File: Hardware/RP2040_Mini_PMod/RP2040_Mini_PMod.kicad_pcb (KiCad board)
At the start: 4 copper layers, 50 x 20 mm, 39 parts, among them J3 Conn_02x06_Odd_Even, J4 USB_C_Receptacle_USB2.0, J5 Conn_01x04, SW1 SW_Push, SW2 SW_Push, U1 RP2040, U2 W25Q128JVS, U3 NCP1117-3.3_SOT223, Y1 12MHz

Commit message: continue with mini project
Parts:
- added J1: Micro_SD_Card, jjh:105162-0001, B.Cu at (149.5, 104.2)
- SW1, SW2: footprint Button_Switch_THT:SW_PUSH_6mm_H4.3mm -> jjh:PTS815SJK250SMTRLFS
- moved SW2 54.8 mm to (166.9, 111.7)
- moved SW1 31.1 mm to (166.9, 96.4)
- moved R2 27.3 mm to (162.9, 96.6), turned to 90 degrees
- moved J3 9.30 mm to (172.3, 97.3)
- moved C2 5.61 mm to (168.5, 107.9), turned to 180 degrees
- moved R1 4.95 mm to (168.5, 100.3), turned to 180 degrees
- moved C4 4.95 mm to (168.5, 101.9)
- moved Y1 1.36 mm to (168.5, 104.9), turned to 90 degrees
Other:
- board size 50 x 20 mm -> 40 x 20 mm

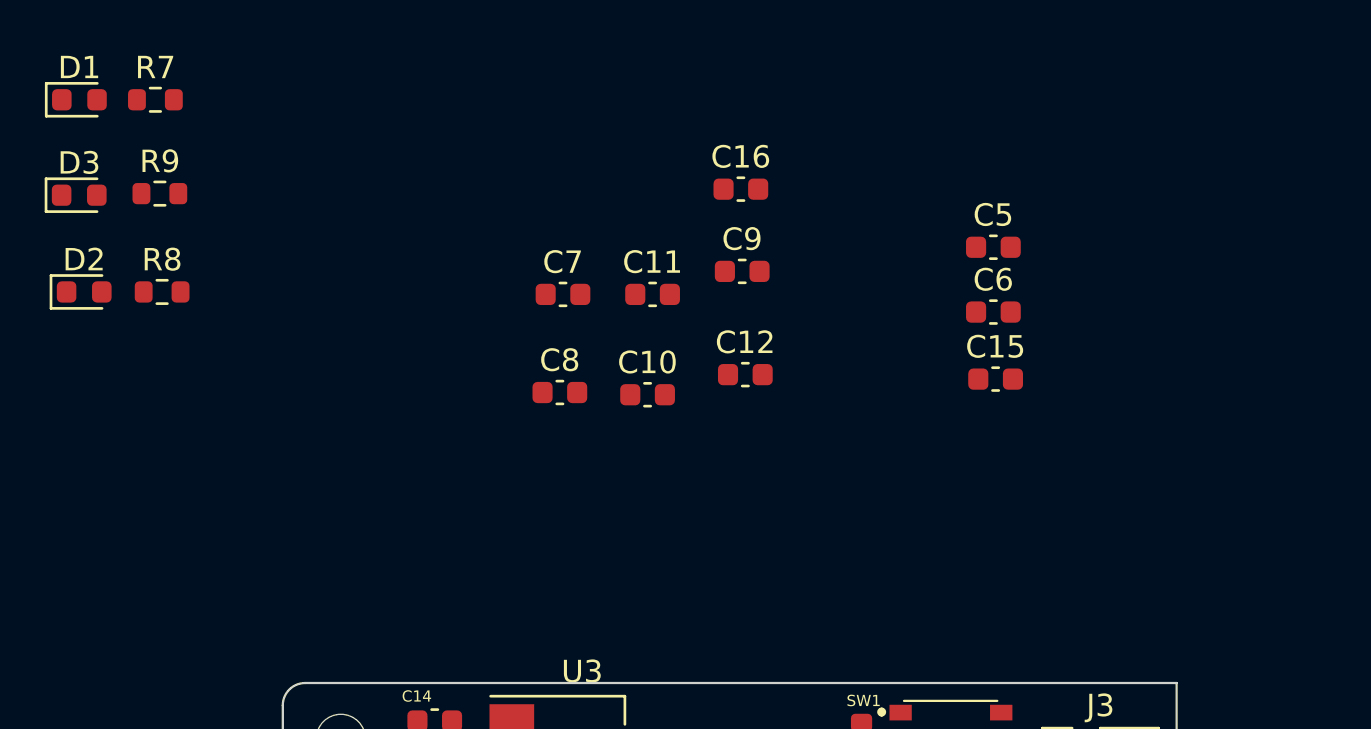
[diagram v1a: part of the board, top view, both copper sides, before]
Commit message: Add the SD GPIO and RGB LED to schematic
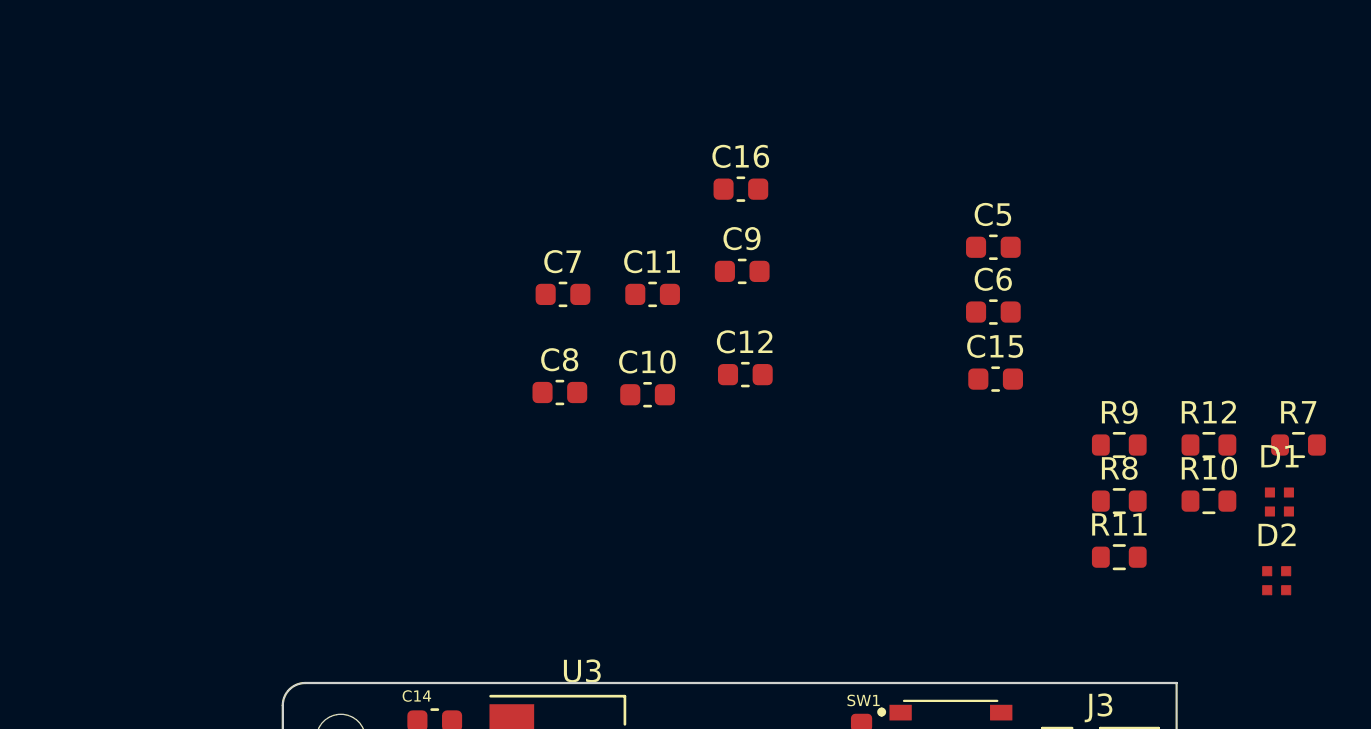
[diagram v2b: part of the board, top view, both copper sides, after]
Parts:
- removed D3: LED, LED_SMD:LED_0603_1608Metric
- added R10: 160, Resistor_SMD:R_0603_1608Metric, F.Cu at (178.4, 85.9)
- added R11: 80, Resistor_SMD:R_0603_1608Metric, F.Cu at (174.4, 88.4)
- added R12: 80, Resistor_SMD:R_0603_1608Metric, F.Cu at (178.4, 83.3)
- D1, D2: value LED -> LED_ARGB; footprint LED_SMD:LED_0603_1608Metric -> jjh:SX-0402-RGB
- R7: value 330 -> 160
- R8, R9: value 330 -> 80
- SW1, SW2: value SW_Push -> PTS815 SJK 250 SMTR LFS
- moved D1 56.6 mm to (181.6, 85.9)
- moved D2 54.9 mm to (181.5, 89.4)
- moved R7 53.4 mm to (182.5, 83.3)
- moved R9 44.4 mm to (174.4, 83.3)
- moved R8 43.8 mm to (174.4, 85.9)
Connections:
- J1 pad 2: unconnected-(J1-Pad2) -> GPIO_17
- J1 pad 3: unconnected-(J1-Pad3) -> GPIO_19
- J1 pad 4: unconnected-(J1-Pad4) -> +3V3
- J1 pad 5: unconnected-(J1-Pad5) -> GPIO_18
- J1 pad 6: unconnected-(J1-Pad6) -> GND
- J1 pad 7: unconnected-(J1-Pad7) -> GPIO_16
- J1 pad 9: unconnected-(J1-Pad9) -> GND
- R7 pad 1: GPIO_24 -> GPIO_8
- R7 pad 2: Net-(D1-Pad2) -> Net-(D1-Pad4)
- R8 pad 1: GPIO_25 -> GPIO_9
- R8 pad 2: Net-(D2-Pad2) -> Net-(D1-Pad3)
- R9 pad 1: +3V3 -> GPIO_10
- R9 pad 2: Net-(D3-Pad2) -> Net-(D1-Pad2)

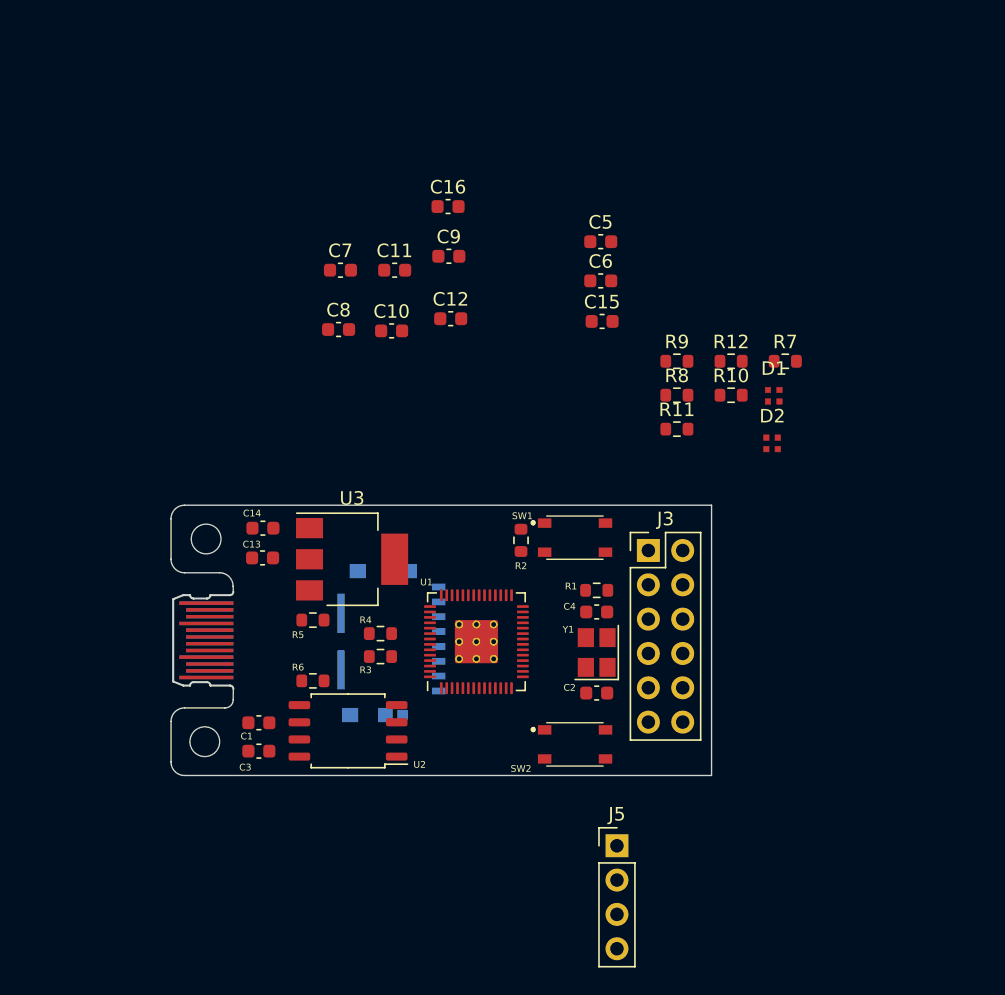
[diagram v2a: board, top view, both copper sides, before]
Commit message: complete schematic and start pcb routing
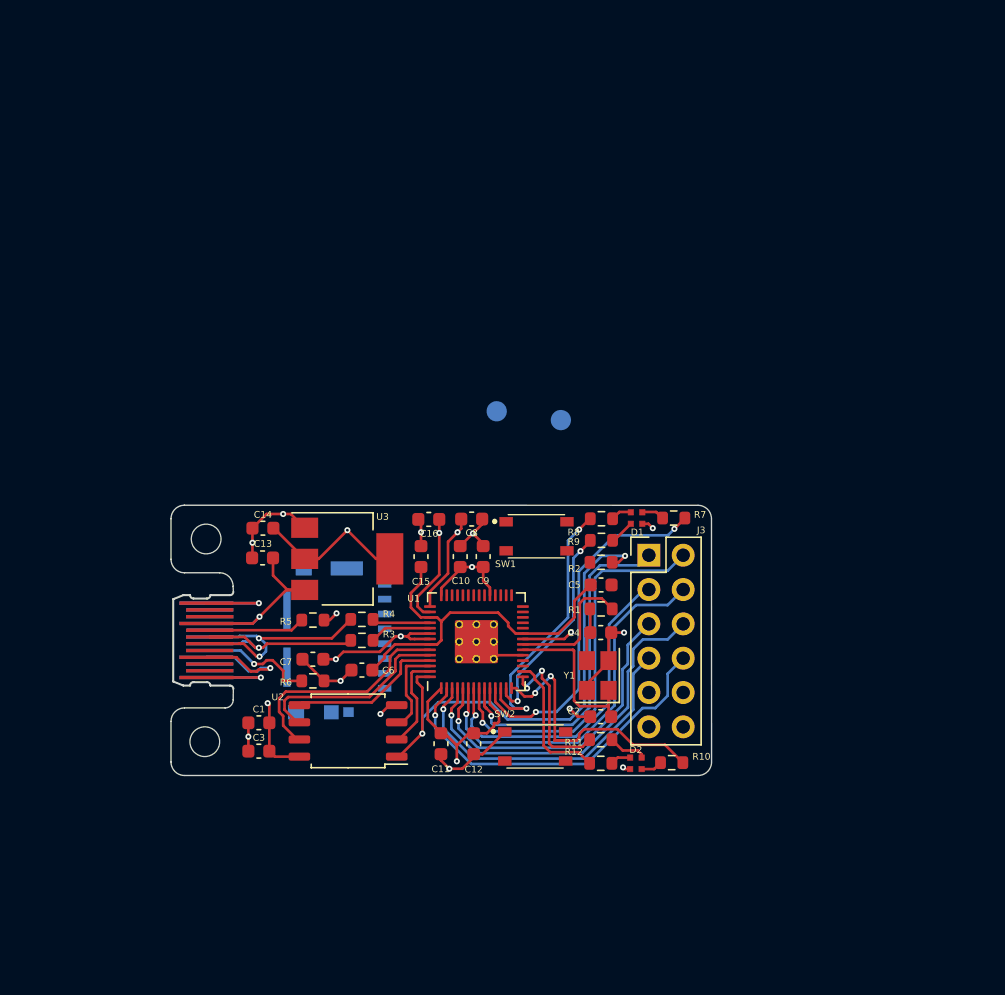
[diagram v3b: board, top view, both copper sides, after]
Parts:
- removed J5: Conn_01x04, Connector_PinHeader_2.54mm:PinHeader_1x04_P2.54mm_Vertical
- added TP1: TestPoint, TestPoint:TestPoint_Pad_D1.5mm, B.Cu at (161.1, 87.0)
- added TP2: TestPoint, TestPoint:TestPoint_Pad_D1.5mm, B.Cu at (165.8, 87.7)
- moved C11 35.2 mm to (157.0, 111.7), turned to -90 degrees
- moved C6 33.8 mm to (151.1, 106.2), turned to 180 degrees
- moved C12 31.5 mm to (159.4, 111.7), turned to -90 degrees
- moved R12 31.3 mm to (168.8, 113.1)
- moved C7 28.9 mm to (147.5, 105.4), turned to 180 degrees
- moved R10 27.5 mm to (174.1, 113.0), turned to 180 degrees
- moved D2 25.7 mm to (171.4, 113.1), turned to 180 degrees
- moved C5 25.4 mm to (168.8, 99.9)
- moved R11 23.7 mm to (168.8, 111.3)
- moved C16 23.2 mm to (156.1, 95.0), turned to 180 degrees
- moved C9 22.4 mm to (160.1, 97.8), turned to 90 degrees
- moved C15 22.0 mm to (155.5, 97.8), turned to 90 degrees
- moved C10 17.5 mm to (158.4, 97.8), turned to 90 degrees
- moved C8 17.1 mm to (159.2, 95.0)
- moved R9 14.4 mm to (168.8, 96.6)
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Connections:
- J1 pad 1: unconnected-(J1-Pad1) -> GPIO_21
- J1 pad 8: unconnected-(J1-Pad8) -> GPIO_20
- U1 pad 17: GPIO_14 -> unconnected-(U1-Pad17)
- U1 pad 18: GPIO_15 -> unconnected-(U1-Pad18)
- U1 pad 34: GPIO_22 -> unconnected-(U1-Pad34)
- U1 pad 35: GPIO_23 -> unconnected-(U1-Pad35)
- U1 pad 36: GPIO_24 -> unconnected-(U1-Pad36)
- U1 pad 37: GPIO_25 -> unconnected-(U1-Pad37)
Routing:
- net +3V3: track 0.00 -> 68.3 mm, vias 0 -> 9
- net GND: track 0.00 -> 56.9 mm, vias 0 -> 15
- net QSPI_SS: track 0.00 -> 36.9 mm, vias 0 -> 2
- net VBUS: track 0.00 -> 31.2 mm, vias 0 -> 2
- net GPIO_6: track 0.00 -> 28.9 mm, vias 0 -> 1
- net +1V1: track 0.00 -> 27.8 mm
- net GPIO_4: track 0.00 -> 27.6 mm, vias 0 -> 1
- net GPIO_2: track 0.00 -> 27.4 mm, vias 0 -> 1
- net GPIO_0: track 0.00 -> 27.0 mm, vias 0 -> 1
- net GPIO_8: track 0.00 -> 26.7 mm, vias 0 -> 2
- net GPIO_7: track 0.00 -> 25.6 mm, vias 0 -> 1
- net GPIO_5: track 0.00 -> 24.4 mm, vias 0 -> 1
- net GPIO_1: track 0.00 -> 24.0 mm, vias 0 -> 1
- net GPIO_3: track 0.00 -> 24.0 mm, vias 0 -> 1
- net GPIO_11: track 0.00 -> 20.6 mm, vias 0 -> 2
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- added copper zone on In2.Cu, net +3V3
- added copper zone on In1.Cu, net GND
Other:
- outline, holes or cut-outs redrawn

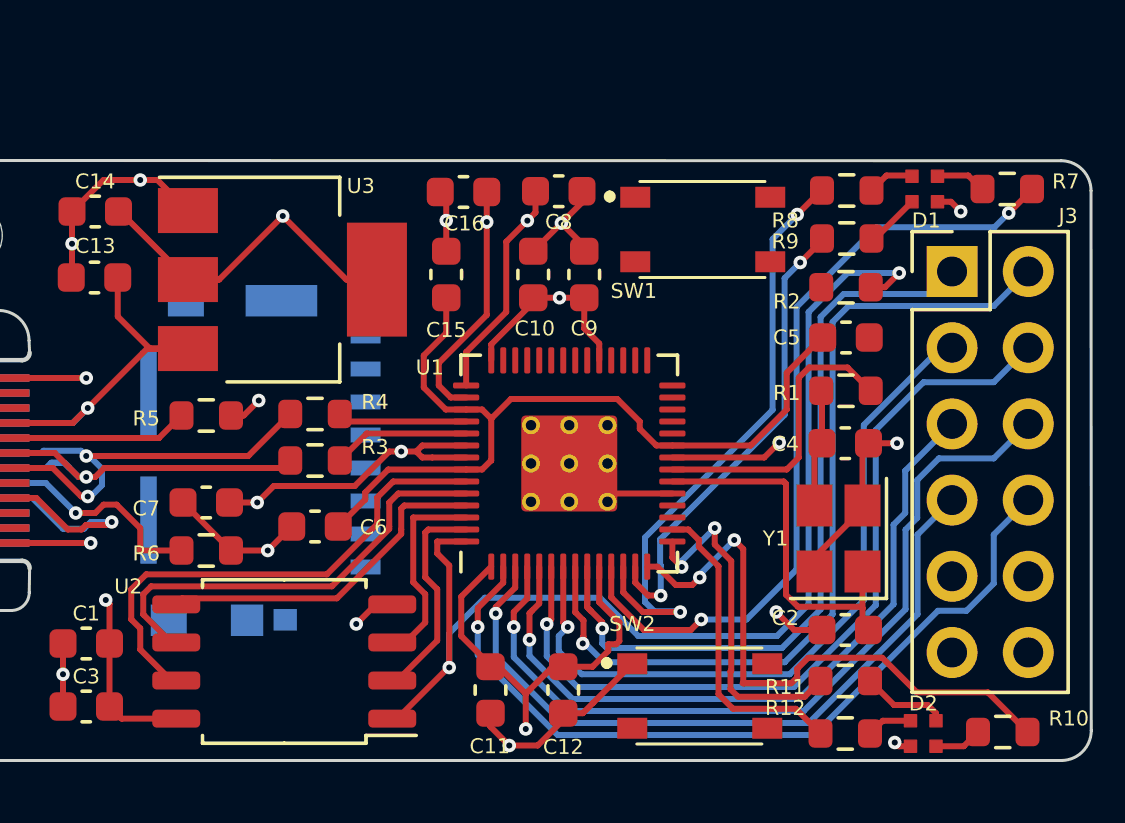
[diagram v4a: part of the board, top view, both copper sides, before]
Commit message: update button footprint and fix some drc errors
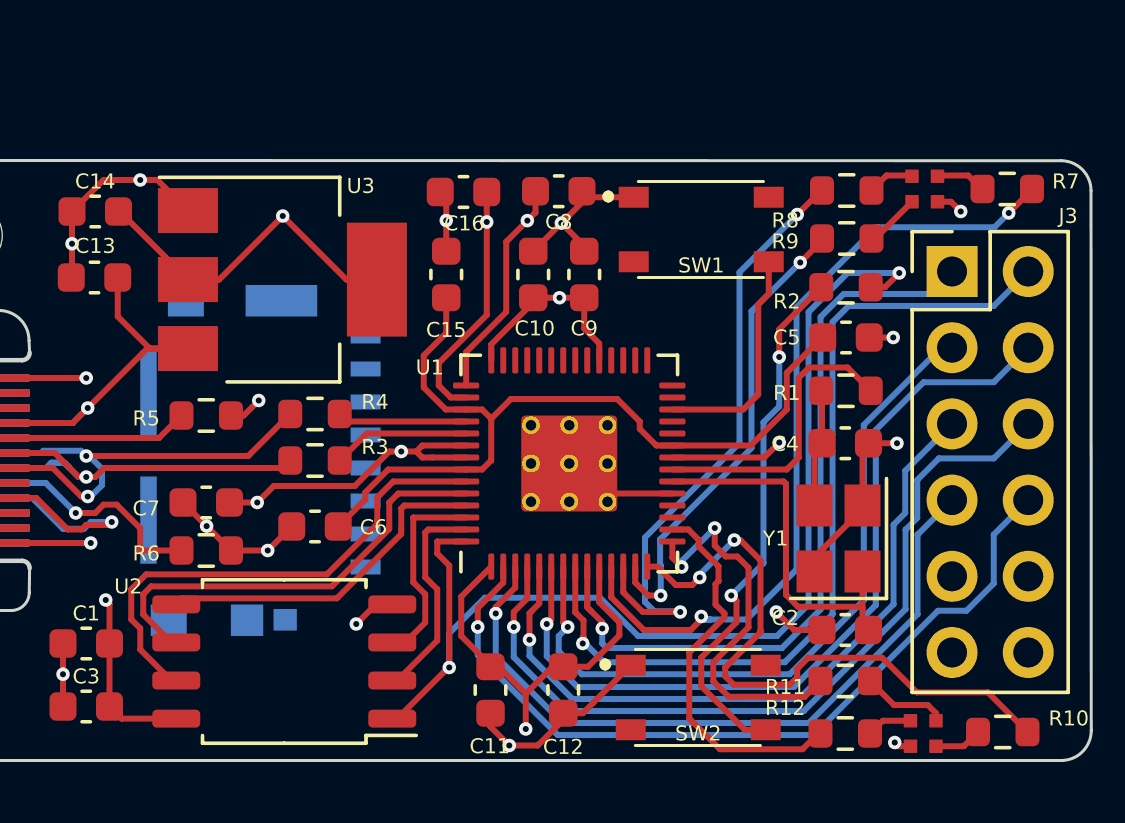
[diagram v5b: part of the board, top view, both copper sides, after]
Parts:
- moved SW2 0.07 mm to (163.9, 111.9)
- moved SW1 0.05 mm to (164.0, 96.3)
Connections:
- SW1 pad 2: Net-(R2-Pad2) -> unconnected-(SW1-Pad2)
- SW1 pad 3: (no net) -> unconnected-(SW1-Pad3)
- SW1 pad 4: (no net) -> Pico_Run
- SW2 pad 2: Pico_Run -> unconnected-(SW2-Pad2)
- SW2 pad 3: (no net) -> unconnected-(SW2-Pad3)
- SW2 pad 4: (no net) -> Net-(R2-Pad2)
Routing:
- net Net-(R2-Pad2): track 0.00 -> 17.9 mm, vias 0 -> 2
- net Pico_Run: track 0.00 -> 7.64 mm
- net GND: track 56.9 -> 59.5 mm, vias 15 -> 17
- net GPIO_13: track 10.4 -> 12.9 mm
- net GPIO_12: track 11.7 -> 13.0 mm
- net GPIO_11: track 20.6 -> 21.1 mm
